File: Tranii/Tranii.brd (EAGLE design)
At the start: 160 x 100 mm, 26 parts

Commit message: finished pin mapping
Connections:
- removed net INT: J1.1
- removed net N$33: U$6.A0
- removed net N$34: U$6.A1
- removed net N$35: U$6.A2
- removed net N$36: U$6.A3
- removed net N$37: U$6.A4
- removed net N$38: U$6.A5
- removed net N$48: U$6.A12
- removed net N$49: U$6.A11
- removed net N$50: U$6.A10
- removed net N$51: U$6.A9
- removed net N$52: U$6.A8
- removed net N$53: U$6.A7
- removed net N$54: U$6.A6
- removed net N$55: U$6.22
- removed net N$56: U$6.23
- removed net N$59: J2.3
- removed net N$64: J3.3
- removed net N$77: U$1.BIN2
- removed net N$78: U$1.BIN1
- removed net N$79: U$1.AIN2
- removed net N$80: U$1.AIN1
- removed net N3: U$2.AIN1
- removed net N75: U$2.AIN2
- new net LEFT_A: U$1.AIN1, U$6.A1
- new net LEFT_B: U$1.AIN2, U$6.A12
- new net LIFT_A: U$2.AIN1, U$6.A7
- new net LIFT_B: U$2.AIN2, U$6.A6
- new net RIGHT_A: U$1.BIN1, U$6.A10
- new net RIGHT_B: U$1.BIN2, U$6.A8
- new net TICKLEFT: J2.3, U$6.A4
- new net TICKRIGHT: J3.3, U$6.A5
- net 5VCC: now also R5.1
- net ECHO: now also U$6.A9
- net N$1: now also R6.1
- net OUT1: now also U$6.A2
- net OUT2: now also U$6.A3
- net SCL: now also U$6.22
- net SDA: now also U$6.23
- net TRIG: now also U$6.A0
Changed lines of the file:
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@@
 <signal name="OUT1">
 <contactref element="J4" pad="3"/>
+<contactref element="U$6" pad="A2"/>
+<wire x1="-128.905" y1="-236.22" x2="-35.56" y2="-118.11" width="0" layer="19" extent="1-1"/>
 </signal>
 <signal name="ECHO">
 <contactref element="J6" pad="3"/>
+<contactref element="U$6" pad="A9"/>
+<wire x1="-109.855" y1="-246.38" x2="-35.56" y2="-156.21" width="0" layer="19" extent="1-1"/>
 </signal>
 <signal name="VCC5">
@@
 <signal name="SCL">
 <contactref element="J1" pad="3"/>
+<contactref element="U$6" pad="22"/>
+<wire x1="-35.56" y1="-60.96" x2="-109.855" y2="-256.54" width="0" layer="19" extent="1-1"/>
 </signal>
 <signal name="SDA">
 <contactref element="J1" pad="2"/>
-</signal>
-<signal name="INT">
-<contactref element="J1" pad="1"/>
+<contactref element="U$6" pad="23"/>
+<wire x1="-38.1" y1="-60.96" x2="-109.855" y2="-259.08" width="0" layer="19" extent="1-1"/>
 </signal>
 <signal name="N$29">
@@
 <signal name="N$30">
 <contactref element="U$6" pad="3V"/>
-</signal>
-<signal name="N$33">
-<contactref element="U$6" pad="A0"/>
-</signal>
-<signal name="N$34">
-<contactref element="U$6" pad="A1"/>
-</signal>
-<signal name="N$35">
-<contactref element="U$6" pad="A2"/>
-</signal>
-<signal name="N$36">
-<contactref element="U$6" pad="A3"/>
-</signal>
-<signal name="N$37">
-<contactref element="U$6" pad="A4"/>
-</signal>
-<signal name="N$38">
-<contactref element="U$6" pad="A5"/>
 </signal>
 <signal name="N$39">
@@
 <contactref element="U$6" pad="USB"/>
 </signal>
-<signal name="N$48">
-<contactref element="U$6" pad="A12"/>
-</signal>
-<signal name="N$49">
-<contactref element="U$6" pad="A11"/>
-</signal>
-<signal name="N$50">
-<contactref element="U$6" pad="A10"/>
-</signal>
-<signal name="N$51">
-<contactref element="U$6" pad="A9"/>
-</signal>
-<signal name="N$52">
-<contactref element="U$6" pad="A8"/>
-</signal>
-<signal name="N$53">
-<contactref element="U$6" pad="A7"/>
-</signal>
-<signal name="N$54">
-<contactref element="U$6" pad="A6"/>
-</signal>
-<signal name="N$55">
-<contactref element="U$6" pad="22"/>
-</signal>
-<signal name="N$56">
-<contactref element="U$6" pad="23"/>
-</signal>
-<signal name="N$59">
+<signal name="TICKLEFT">
 <contactref element="J2" pad="3"/>
+<contactref element="U$6" pad="A4"/>
+<wire x1="-128.905" y1="-241.3" x2="-35.56" y2="-80.01" width="0" layer="19" extent="1-1"/>
 </signal>
 <signal name="LEFT0">
@@
 <wire x1="-61.315" y1="-254.26" x2="-38.1" y2="-175.26" width="0" layer="19" extent="1-1"/>
 </signal>
-<signal name="N$64">
+<signal name="TICKRIGHT">
 <contactref element="J3" pad="3"/>
+<contactref element="U$6" pad="A5"/>
+<wire x1="-128.905" y1="-243.84" x2="-35.56" y2="-99.06" width="0" layer="19" extent="1-1"/>
 </signal>
 <signal name="RIGHT0">
@@
 <wire x1="-54.935" y1="-221.24" x2="-38.1" y2="-213.36" width="0" layer="19" extent="1-1"/>
 </signal>
-<signal name="N$77">
+<signal name="RIGHT_B">
 <contactref element="U$1" pad="BIN2"/>
+<contactref element="U$6" pad="A8"/>
+<wire x1="-58.065" y1="-248.66" x2="-109.855" y2="-248.92" width="0" layer="19" extent="1-1"/>
 </signal>
-<signal name="N$78">
+<signal name="RIGHT_A">
 <contactref element="U$1" pad="BIN1"/>
+<contactref element="U$6" pad="A10"/>
+<wire x1="-57.415" y1="-248.66" x2="-109.855" y2="-243.84" width="0" layer="19" extent="1-1"/>
 </signal>
-<signal name="N$79">
+<signal name="LEFT_B">
 <contactref element="U$1" pad="AIN2"/>
+<contactref element="U$6" pad="A12"/>
+<wire x1="-61.315" y1="-248.66" x2="-109.855" y2="-238.76" width="0" layer="19" extent="1-1"/>
 </signal>
-<signal name="N$80">
+<signal name="LEFT_A">
 <contactref element="U$1" pad="AIN1"/>
+<contactref element="U$6" pad="A1"/>
+<wire x1="-61.965" y1="-248.66" x2="-128.905" y2="-233.68" width="0" layer="19" extent="1-1"/>
 </signal>
 <signal name="OUT2">
 <contactref element="J5" pad="3"/>
+<contactref element="U$6" pad="A3"/>
+<wire x1="-128.905" y1="-238.76" x2="-35.56" y2="-137.16" width="0" layer="19" extent="1-1"/>
 </signal>
 <signal name="TRIG">
 <contactref element="J6" pad="2"/>
+<contactref element="U$6" pad="A0"/>
+<wire x1="-128.905" y1="-231.14" x2="-38.1" y2="-156.21" width="0" layer="19" extent="1-1"/>
 </signal>
 <signal name="5VCC">
 <contactref element="U$8" pad="VOUT"/>
 <contactref element="C6" pad="1"/>
+<contactref element="R5" pad="1"/>
+<wire x1="-135.57" y1="-275.59" x2="-142.24" y2="-281.94" width="0" layer="19" extent="1-1"/>
 <wire x1="-138.43" y1="-270.825" x2="-135.57" y2="-275.59" width="0" layer="19" extent="1-1"/>
 </signal>
@@
 <contactref element="R5" pad="2"/>
 <contactref element="U$8" pad="FB"/>
+<contactref element="R6" pad="1"/>
+<wire x1="-139.7" y1="-281.94" x2="-142.24" y2="-288.29" width="0" layer="19" extent="1-1"/>
 <wire x1="-137.48" y1="-270.825" x2="-139.7" y2="-281.94" width="0" layer="19" extent="1-1"/>
 </signal>
-<signal name="N3">
+<signal name="LIFT_A">
 <contactref element="U$2" pad="AIN1"/>
+<contactref element="U$6" pad="A7"/>
+<wire x1="-56.885" y1="-215.64" x2="-109.855" y2="-251.46" width="0" layer="19" extent="1-1"/>
 </signal>
-<signal name="N75">
+<signal name="LIFT_B">
 <contactref element="U$2" pad="AIN2"/>
+<contactref element="U$6" pad="A6"/>
+<wire x1="-56.235" y1="-215.64" x2="-109.855" y2="-254" width="0" layer="19" extent="1-1"/>
 </signal>
 </signals>

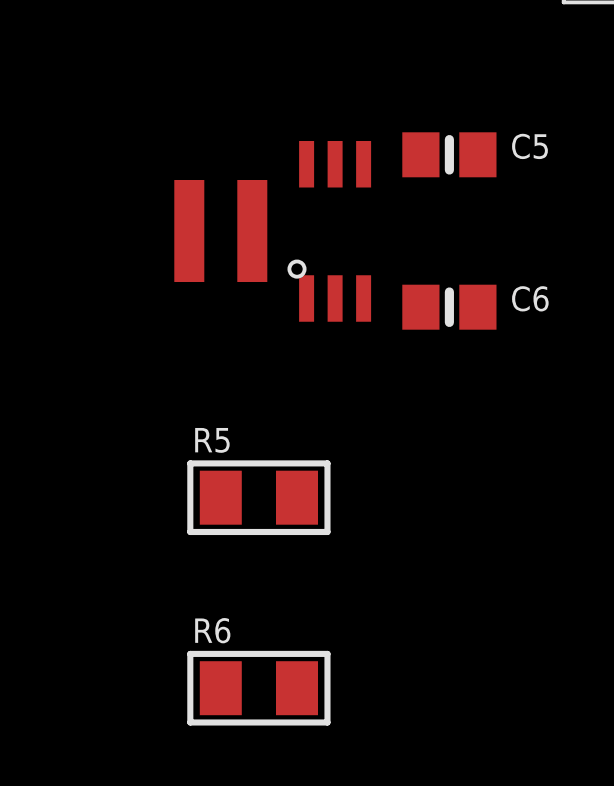
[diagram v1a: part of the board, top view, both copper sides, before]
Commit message: cleaned up schematic
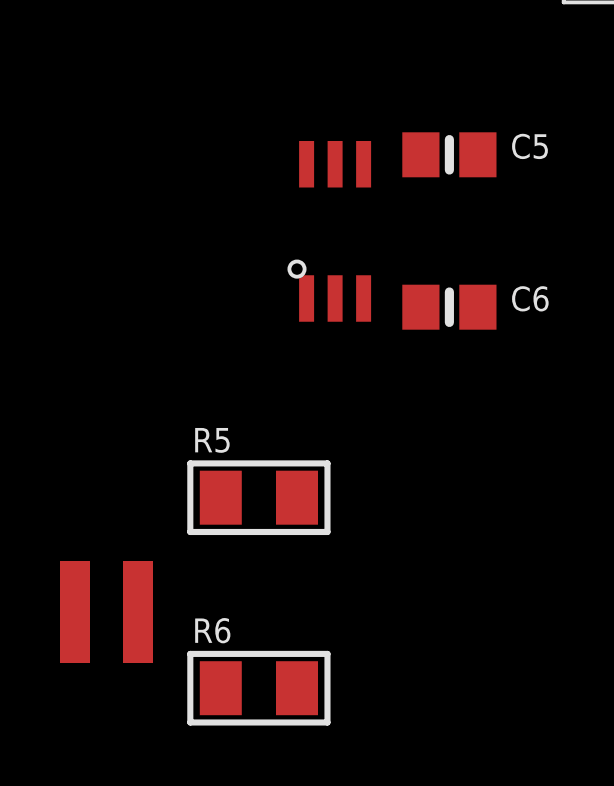
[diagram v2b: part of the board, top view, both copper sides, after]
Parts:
- J1: value (none) -> apd
- J2: value (none) -> left motor encoder
- J3: value (none) -> right motor encoder
- J4: value (none) -> line sensor 2
- J5: value (none) -> line sensor 1
- J6: value (none) -> ultrasonic
- J7: value (none) -> left motor output
- J8: value (none) -> right motor output
- J9: value (none) -> lift motor output
- moved U$11 13.3 mm to (-146.1, -285.8)
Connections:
- removed net 5VCC: C6.1, R5.1, U$8.VOUT
- removed net N$2 (its old number): U$8.GND
- removed net N$29: U$6.RST
- removed net N$30: U$6.3V
- removed net N$39: U$6.SCK
- removed net N$40: U$6.MO
- removed net N$41: U$6.MI
- removed net N$42: U$6.RX
- removed net N$43: U$6.TX
- removed net N$44: U$6.21
- removed net N$46: U$6.EN
- removed net N$47: U$6.USB
- net GND: now also U$8.GND
- net VCC5: now also C6.1, R5.1, U$8.VOUT
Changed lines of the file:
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@@
 </autorouter>
 <elements>
-<element name="J1" library="SparkFun-Connectors" library_urn="urn:adsk.eagle:library:513" package="1X06" package3d_urn="urn:adsk.eagle:package:38009/1" value="" x="-40.64" y="-60.96">
+<element name="J1" library="SparkFun-Connectors" library_urn="urn:adsk.eagle:library:513" package="1X06" package3d_urn="urn:adsk.eagle:package:38009/1" value="apd" x="-40.64" y="-60.96">
 <attribute name="PROD_ID" value="CONN-08437" x="-40.64" y="-60.96" size="1.778" layer="27" display="off"/>
 </element>
-<element name="J2" library="SparkFun-Connectors" library_urn="urn:adsk.eagle:library:513" package="1X03" package3d_urn="urn:adsk.eagle:package:38063/1" value="" x="-40.64" y="-80.01"/>
-<element name="J3" library="SparkFun-Connectors" library_urn="urn:adsk.eagle:library:513" package="1X03" package3d_urn="urn:adsk.eagle:package:38063/1" value="" x="-40.64" y="-99.06"/>
-<element name="J4" library="SparkFun-Connectors" library_urn="urn:adsk.eagle:library:513" package="1X03" package3d_urn="urn:adsk.eagle:package:38063/1" value="" x="-40.64" y="-118.11"/>
-<element name="J5" library="SparkFun-Connectors" library_urn="urn:adsk.eagle:library:513" package="1X03" package3d_urn="urn:adsk.eagle:package:38063/1" value="" x="-40.64" y="-137.16"/>
-<element name="J6" library="SparkFun-Connectors" library_urn="urn:adsk.eagle:library:513" package="1X04" package3d_urn="urn:adsk.eagle:package:38085/1" value="" x="-40.64" y="-156.21">
+<element name="J2" library="SparkFun-Connectors" library_urn="urn:adsk.eagle:library:513" package="1X03" package3d_urn="urn:adsk.eagle:package:38063/1" value="left motor encoder" x="-40.64" y="-80.01"/>
+<element name="J3" library="SparkFun-Connectors" library_urn="urn:adsk.eagle:library:513" package="1X03" package3d_urn="urn:adsk.eagle:package:38063/1" value="right motor encoder" x="-40.64" y="-99.06"/>
+<element name="J4" library="SparkFun-Connectors" library_urn="urn:adsk.eagle:library:513" package="1X03" package3d_urn="urn:adsk.eagle:package:38063/1" value="line sensor 2" x="-40.64" y="-118.11"/>
+<element name="J5" library="SparkFun-Connectors" library_urn="urn:adsk.eagle:library:513" package="1X03" package3d_urn="urn:adsk.eagle:package:38063/1" value="line sensor 1" x="-40.64" y="-137.16"/>
+<element name="J6" library="SparkFun-Connectors" library_urn="urn:adsk.eagle:library:513" package="1X04" package3d_urn="urn:adsk.eagle:package:38085/1" value="ultrasonic" x="-40.64" y="-156.21">
 <attribute name="PROD_ID" value="CONN-09696" x="-40.64" y="-156.21" size="1.778" layer="27" display="off"/>
 </element>
-<element name="J7" library="SparkFun-Connectors" library_urn="urn:adsk.eagle:library:513" package="1X02" package3d_urn="urn:adsk.eagle:package:38039/1" value="" x="-40.64" y="-175.26"/>
-<element name="J8" library="SparkFun-Connectors" library_urn="urn:adsk.eagle:library:513" package="1X02" package3d_urn="urn:adsk.eagle:package:38039/1" value="" x="-40.64" y="-194.31"/>
-<element name="J9" library="SparkFun-Connectors" library_urn="urn:adsk.eagle:library:513" package="1X02" package3d_urn="urn:adsk.eagle:package:38039/1" value="" x="-40.64" y="-213.36"/>
+<element name="J7" library="SparkFun-Connectors" library_urn="urn:adsk.eagle:library:513" package="1X02" package3d_urn="urn:adsk.eagle:package:38039/1" value="left motor output" x="-40.64" y="-175.26"/>
+<element name="J8" library="SparkFun-Connectors" library_urn="urn:adsk.eagle:library:513" package="1X02" package3d_urn="urn:adsk.eagle:package:38039/1" value="right motor output" x="-40.64" y="-194.31"/>
+<element name="J9" library="SparkFun-Connectors" library_urn="urn:adsk.eagle:library:513" package="1X02" package3d_urn="urn:adsk.eagle:package:38039/1" value="lift motor output" x="-40.64" y="-213.36"/>
 <element name="U$2" library="Tranii" package="DRV8833" value="DRV8833" x="-54.61" y="-218.44"/>
 <element name="C2" library="microbuilder" package="0805-NO" value="0.1uF" x="-60.96" y="-226.06"/>
@@
 <element name="C6" library="microbuilder" package="0805-NO" value="10µF" x="-134.62" y="-275.59"/>
 <element name="U$8" library="Tranii" package="TLV61220" value="LPV61220" x="-138.43" y="-273.05"/>
-<element name="U$11" library="Tranii" package="VLS3012HBX" value="VLS3012HBX" x="-142.24" y="-273.05"/>
 <element name="R5" library="microbuilder" package="_1206" value="0.2Ω" x="-140.97" y="-281.94"/>
 <element name="R6" library="microbuilder" package="_1206" value="0.2Ω" x="-140.97" y="-288.29"/>
+<element name="U$11" library="Tranii" package="VLS3012HBX" value="VLS3012HBX" x="-146.05" y="-285.75"/>
 </elements>
 <signals>
@@
 <contactref element="C6" pad="2"/>
 <contactref element="R6" pad="2"/>
+<contactref element="U$8" pad="GND"/>
 <wire x1="-40.64" y1="-137.16" x2="-33.02" y2="-156.21" width="0" layer="19" extent="1-1"/>
 <wire x1="-40.64" y1="-118.11" x2="-40.64" y2="-137.16" width="0" layer="19" extent="1-1"/>
@@
 <wire x1="-133.67" y1="-270.51" x2="-128.905" y2="-228.6" width="0" layer="19" extent="1-1"/>
 <wire x1="-133.67" y1="-275.59" x2="-133.67" y2="-270.51" width="0" layer="19" extent="1-1"/>
-<wire x1="-139.7" y1="-288.29" x2="-133.67" y2="-275.59" width="0" layer="19" extent="1-1"/>
+<wire x1="-138.43" y1="-275.3" x2="-133.67" y2="-275.59" width="0" layer="19" extent="1-1"/>
+<wire x1="-139.7" y1="-288.29" x2="-138.43" y2="-275.3" width="0" layer="19" extent="1-1"/>
 </signal>
 <signal name="N$3">
@@
 <wire x1="-135.57" y1="-270.51" x2="-109.855" y2="-231.14" width="0" layer="19" extent="1-1"/>
 <wire x1="-139.38" y1="-270.825" x2="-135.57" y2="-270.51" width="0" layer="19" extent="1-1"/>
-<wire x1="-141.19" y1="-273.05" x2="-139.38" y2="-270.825" width="0" layer="19" extent="1-1"/>
-<wire x1="-137.48" y1="-275.3" x2="-141.19" y2="-273.05" width="0" layer="19" extent="1-1"/>
+<wire x1="-137.48" y1="-275.3" x2="-139.38" y2="-270.825" width="0" layer="19" extent="1-1"/>
+<wire x1="-145" y1="-285.75" x2="-137.48" y2="-275.3" width="0" layer="19" extent="1-1"/>
 </signal>
 <signal name="OUT1">
@@
 <signal name="VCC5">
 <contactref element="J6" pad="1"/>
+<contactref element="U$8" pad="VOUT"/>
+<contactref element="C6" pad="1"/>
+<contactref element="R5" pad="1"/>
+<wire x1="-138.43" y1="-270.825" x2="-40.64" y2="-156.21" width="0" layer="19" extent="1-1"/>
+<wire x1="-135.57" y1="-275.59" x2="-138.43" y2="-270.825" width="0" layer="19" extent="1-1"/>
+<wire x1="-142.24" y1="-281.94" x2="-135.57" y2="-275.59" width="0" layer="19" extent="1-1"/>
 </signal>
 <signal name="SCL">
@@
 <wire x1="-38.1" y1="-60.96" x2="-109.855" y2="-259.08" width="0" layer="19" extent="1-1"/>
 </signal>
-<signal name="N$29">
-<contactref element="U$6" pad="RST"/>
-</signal>
-<signal name="N$30">
-<contactref element="U$6" pad="3V"/>
-</signal>
-<signal name="N$39">
-<contactref element="U$6" pad="SCK"/>
-</signal>
-<signal name="N$40">
-<contactref element="U$6" pad="MO"/>
-</signal>
-<signal name="N$41">
-<contactref element="U$6" pad="MI"/>
-</signal>
-<signal name="N$42">
-<contactref element="U$6" pad="RX"/>
-</signal>
-<signal name="N$43">
-<contactref element="U$6" pad="TX"/>
-</signal>
-<signal name="N$44">
-<contactref element="U$6" pad="21"/>
-</signal>
-<signal name="N$46">
-<contactref element="U$6" pad="EN"/>
-</signal>
-<signal name="N$47">
-<contactref element="U$6" pad="USB"/>
-</signal>
 <signal name="TICKLEFT">
 <contactref element="J2" pad="3"/>
@@
 <contactref element="U$6" pad="A0"/>
 <wire x1="-128.905" y1="-231.14" x2="-38.1" y2="-156.21" width="0" layer="19" extent="1-1"/>
-</signal>
-<signal name="5VCC">
-<contactref element="U$8" pad="VOUT"/>
-<contactref element="C6" pad="1"/>
-<contactref element="R5" pad="1"/>
-<wire x1="-135.57" y1="-275.59" x2="-142.24" y2="-281.94" width="0" layer="19" extent="1-1"/>
-<wire x1="-138.43" y1="-270.825" x2="-135.57" y2="-275.59" width="0" layer="19" extent="1-1"/>
-</signal>
-<signal name="N$2">
-<contactref element="U$8" pad="GND"/>
-</signal>
-<signal name="N$11">
-<contactref element="U$11" pad="P$1"/>
-<contactref element="U$8" pad="SW"/>
-<wire x1="-139.38" y1="-275.3" x2="-143.29" y2="-273.05" width="0" layer="19" extent="1-1"/>
 </signal>
 <signal name="N$1">
@@
 <wire x1="-56.235" y1="-215.64" x2="-109.855" y2="-254" width="0" layer="19" extent="1-1"/>
 </signal>
+<signal name="N$2">
+<contactref element="U$11" pad="P$1"/>
+<contactref element="U$8" pad="SW"/>
+<wire x1="-139.38" y1="-275.3" x2="-147.1" y2="-285.75" width="0" layer="19" extent="1-1"/>
+</signal>
 </signals>

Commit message: finished schematic
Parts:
- removed U$11: VLS3012HBX, Tranii:VLS3012HBX
- added R7: 47Ω, microbuilder:_1206
- added R8: 91Ω, microbuilder:_1206
- added U$12: VLS3012HBX, Tranii:VLS3012HBX
- added U$9: LM3671, Tranii:LM3671
- C5: value 10µF -> 4.7uF
- C6: value 10µF -> 10uF
- R5, R6: value 0.2Ω -> 10kΩ
- U$8: value LPV61220 -> BSS138; device Tranii:TLV61220 -> Tranii:BSS138
- moved C1 309.7 mm to (90.2, 14.0)
- moved C2 309.7 mm to (85.1, 47.0)
- moved C4 309.7 mm to (85.1, 7.62)
- moved J1 309.7 mm to (105.4, 212.1)
- moved J2 309.7 mm to (105.4, 193.0)
- moved J3 309.7 mm to (105.4, 174.0)
- moved J4 309.7 mm to (105.4, 154.9)
- moved J6 309.7 mm to (105.4, 116.8)
- moved J7 309.7 mm to (105.4, 97.8)
- moved J8 309.7 mm to (105.4, 78.7)
- moved J9 309.7 mm to (105.4, 59.7)
- moved R1 309.7 mm to (85.1, 35.6)
- moved R2 309.7 mm to (85.1, 29.2)
- moved R3 309.7 mm to (92.7, 22.9)
- moved R4 309.7 mm to (85.1, 14.0)
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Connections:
- new net 3V: J2.1, J3.1, J4.2, J5.2, U$6.3V
- new net ECHO3.3: R7.2, R8.1, U$6.A9
- new net TRIG3.3: R5.2, U$6.A0, U$8.S
- net ECHO: now also R7.1; no longer U$6.A9
- net GND: now also R8.2, U$9.GND; no longer R6.2, U$8.GND
- net N$1: now also U$12.P$1, U$9.SW; no longer R5.2, R6.1, U$8.FB
- net N$2: now also C6.1, U$12.P$2, U$9.FB; no longer U$11.P$1, U$8.SW
- net TRIG: now also R6.2, U$8.D; no longer U$6.A0
- net VCC: now also R5.1, U$8.G, U$9.EN, U$9.VIN; no longer J2.1, J3.1, J4.2, J5.2, U$11.P$2, U$8.EN, U$8.VBAT
- net VCC5: now also R6.1; no longer C6.1, R5.1, U$8.VOUT
